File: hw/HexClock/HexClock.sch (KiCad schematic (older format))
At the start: 30 parts

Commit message: annotated schematic
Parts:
- gave numbers to parts that had none: 30

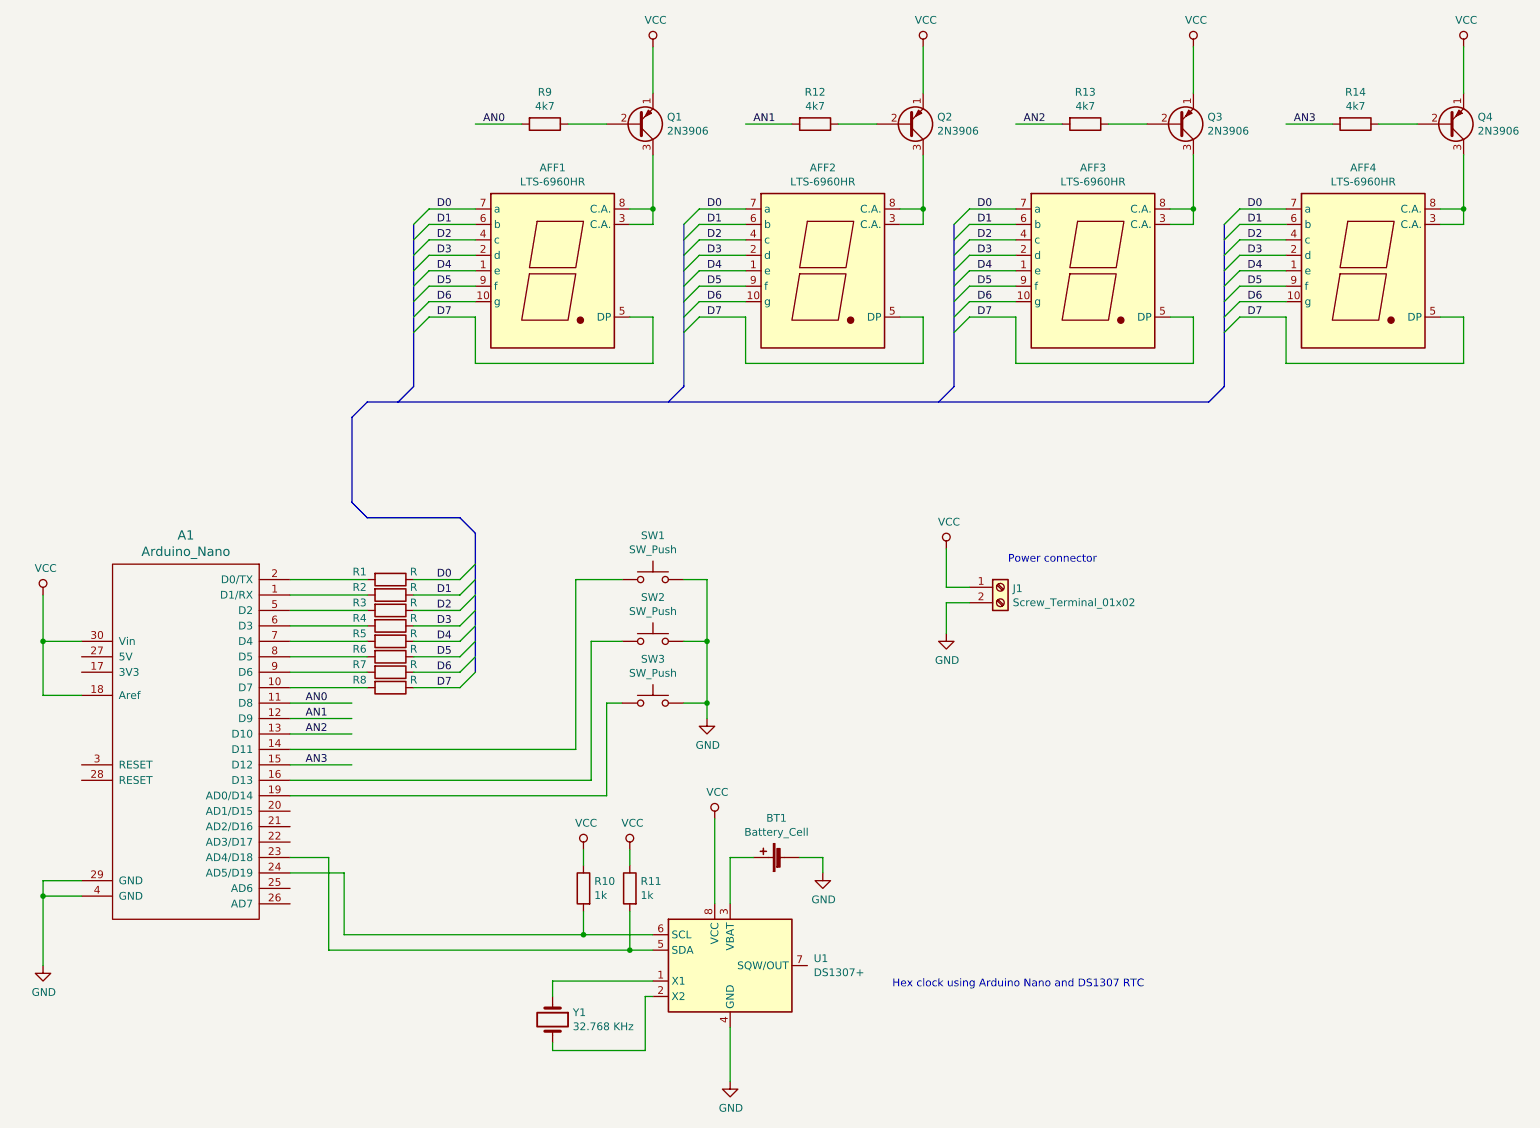
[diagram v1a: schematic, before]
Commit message: use Arduino Nano symbol that has correct pinout
arduino_nano.lib has the TX and RX pins swapped
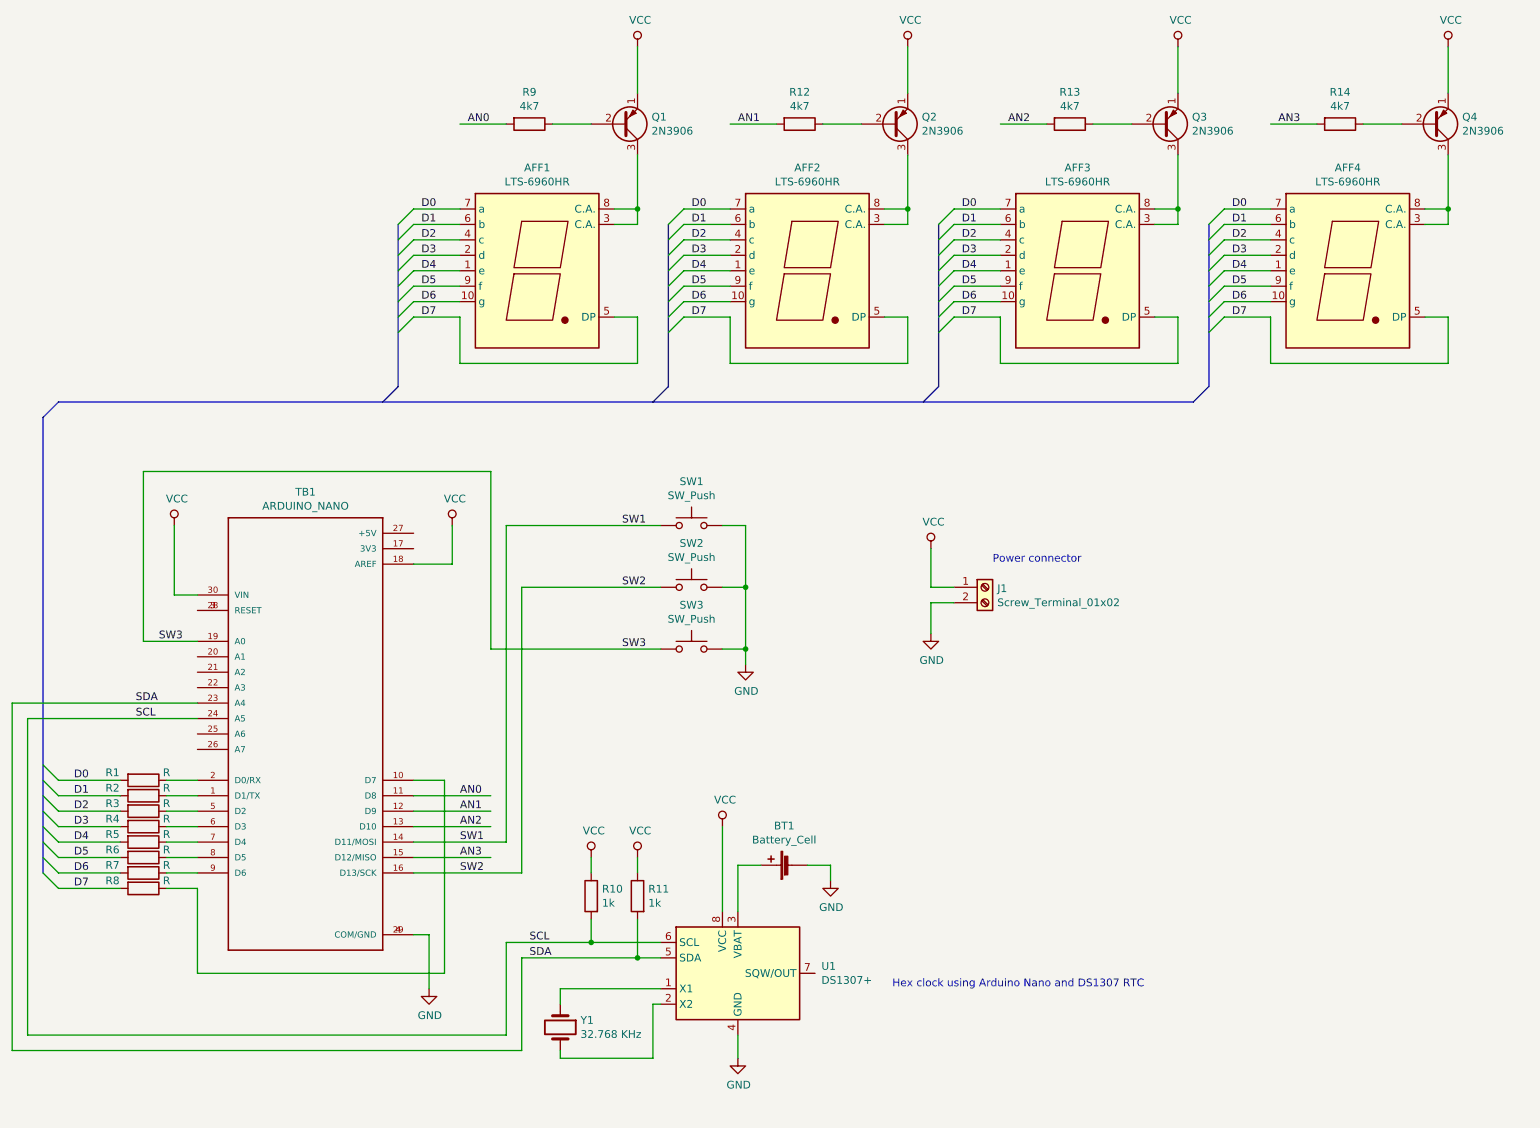
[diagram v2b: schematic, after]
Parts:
- removed A1: Arduino_Nano, symbol arduino_nano:Arduino_Nano
- added TB1: ARDUINO_NANO, SHIELD_ARDUINO_NANO, symbol ARDUINO_NANO:ARDUINO_NANO
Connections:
- net labels added: SCL, SDA, SW1, SW2, SW3
- wire segments 147 -> 155
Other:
- moved on the sheet: AFF1, AFF2, AFF3, AFF4, BT1, J1, Q1, Q2, Q3, Q4, R1, R10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

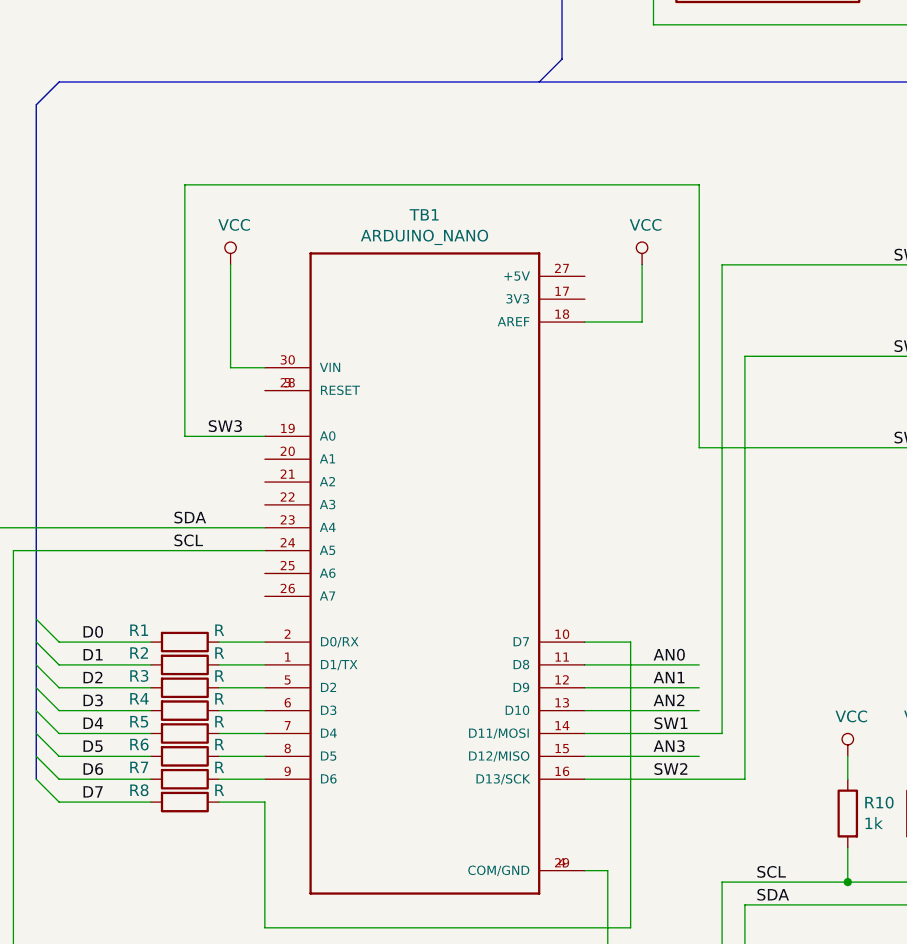
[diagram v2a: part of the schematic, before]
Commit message: After bugfixes, seems to be working
Removed the for loop from the loop() function. (Duh.)

Button 2 is now connected to A1 rather than D13: the
LED and resistor connected to D13 makes it unsuitable
as a digital input.

Still need to clean up the code.
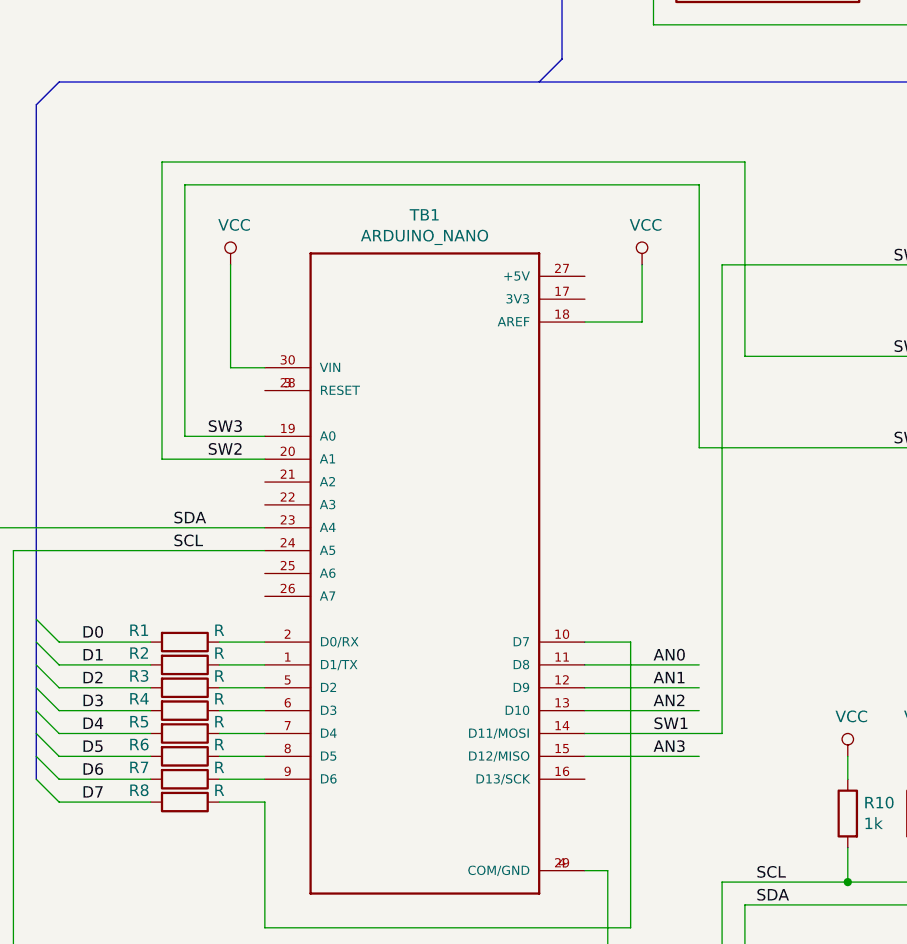
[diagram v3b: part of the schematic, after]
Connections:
- wire segments 155 -> 157
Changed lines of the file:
@@
 EESchema Schematic File Version 4
-LIBS:HexClock-cache
 EELAYER 26 0
 EELAYER END
@@
 	3850 3950 4850 3950
 Wire Wire Line
-	3950 4350 3950 6200
-Wire Wire Line
-	3950 6200 3250 6200
-Wire Wire Line
 	3950 4350 4850 4350
 Wire Wire Line
@@
 Text Label 3550 6000 0    50   ~ 0
 SW1
-Text Label 3550 6200 0    50   ~ 0
+Text Label 1600 4800 0    50   ~ 0
 SW2
 Text Label 1600 4700 0    50   ~ 0
@@
 	1    0    0    -1
 $EndComp
+Wire Wire Line
+	3950 4350 3950 3500
+Wire Wire Line
+	3950 3500 1400 3500
+Wire Wire Line
+	1400 3500 1400 4800
+Wire Wire Line
+	1400 4800 1850 4800
 Wire Bus Line
 	950  3150 8300 3150
